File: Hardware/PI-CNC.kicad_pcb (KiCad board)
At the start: 4 copper layers, 65 x 56 mm, 18 parts, among them J3 40HAT, J6 CONN_02X02, J9 CONN_01X02, Q1 DMG2305UX, Q2 DMMT5401, U2 CAT24C32

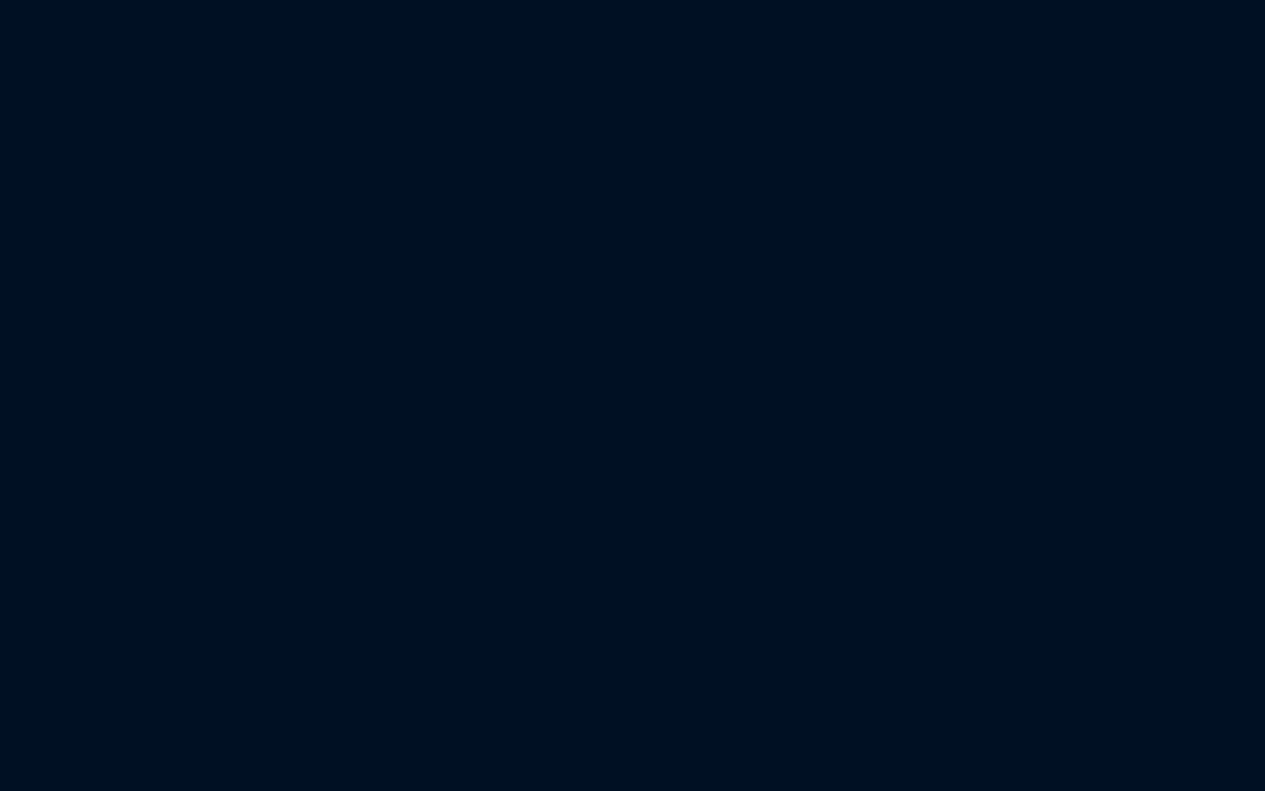
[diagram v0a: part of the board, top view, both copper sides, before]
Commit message: Main Parts on schematic and board.
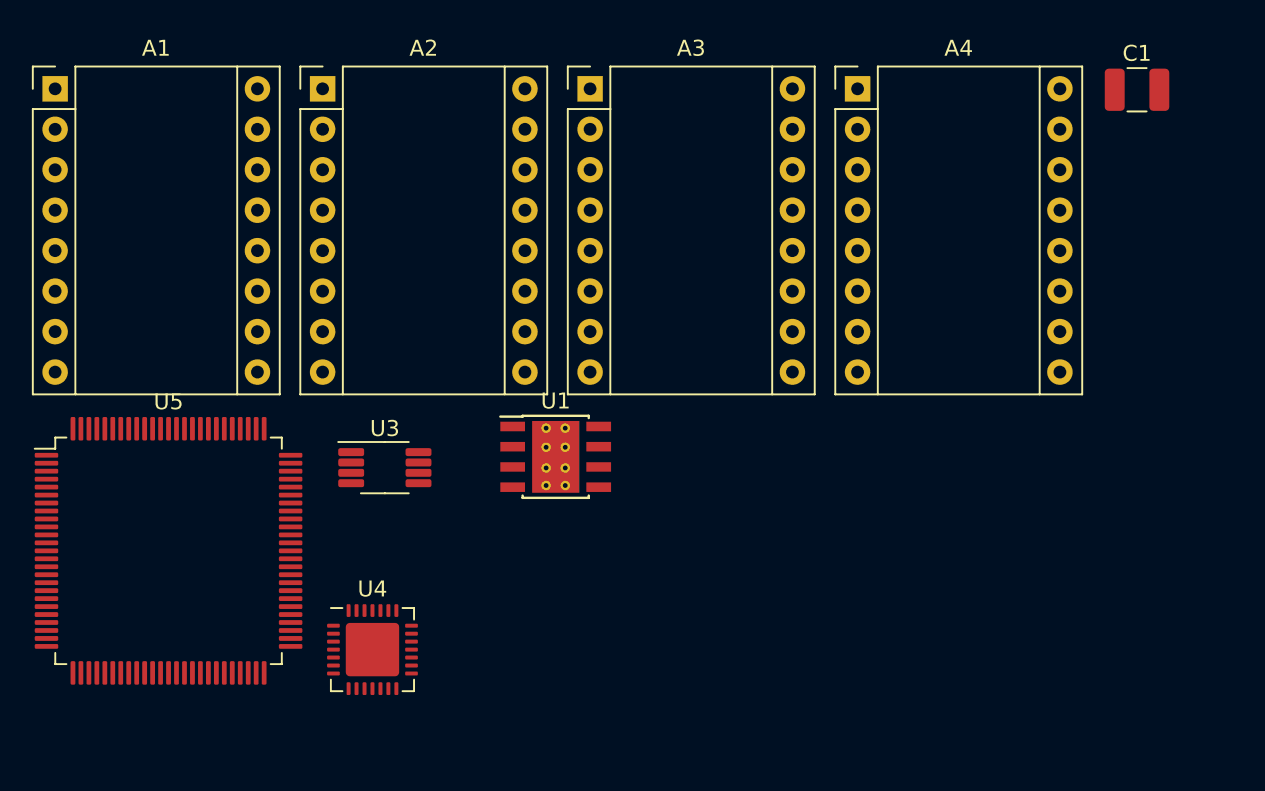
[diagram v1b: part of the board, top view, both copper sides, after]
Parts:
- added A1: Pololu_Breakout_A4988, Module:Pololu_Breakout-16_15.2x20.3mm, F.Cu at (62.6, 18.7)
- added A2: Pololu_Breakout_A4988, Module:Pololu_Breakout-16_15.2x20.3mm, F.Cu at (79.4, 18.7)
- added A3: Pololu_Breakout_A4988, Module:Pololu_Breakout-16_15.2x20.3mm, F.Cu at (96.2, 18.7)
- added A4: Pololu_Breakout_A4988, Module:Pololu_Breakout-16_15.2x20.3mm, F.Cu at (113.0, 18.7)
- added C1: C, Capacitor_SMD:C_1210_3225Metric, F.Cu at (130.5, 18.8)
- added U1: TPS54360DDA, Package_SO:TI_SO-PowerPAD-8_ThermalVias, F.Cu at (94.1, 41.8)
- added U3: DS1339+, Package_SO:MSOP-8_3x3mm_P0.65mm, F.Cu at (83.3, 42.5)
- added U4: CP2102N-A01-GQFN28, Package_DFN_QFN:QFN-28-1EP_5x5mm_P0.5mm_EP3.35x3.35mm, F.Cu at (82.6, 53.9)
- added U5: ATmega2560-16AU, Package_QFP:TQFP-100_14x14mm_P0.5mm, F.Cu at (69.8, 47.7)
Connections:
- J3 pad 10: (no net) -> Console_RX
- J3 pad 11: (no net) -> Net-(J3-Pad11)
- J3 pad 12: (no net) -> LED_white
- J3 pad 13: (no net) -> Net-(J3-Pad13)
- J3 pad 15: (no net) -> Net-(J3-Pad15)
- J3 pad 16: (no net) -> LED_red
- J3 pad 17: (no net) -> Net-(J3-Pad17)
- J3 pad 18: (no net) -> LED_green
- J3 pad 19: (no net) -> Net-(J3-Pad19)
- J3 pad 2: /P5V_HAT -> +5V
- J3 pad 21: (no net) -> Input_SW3
- J3 pad 22: (no net) -> LED_blue
- J3 pad 23: (no net) -> Net-(J3-Pad23)
- J3 pad 24: (no net) -> Net-(J3-Pad24)
- J3 pad 26: (no net) -> Net-(J3-Pad26)
- J3 pad 29: (no net) -> Input_SW2
- J3 pad 3: (no net) -> Net-(J3-Pad3)
- J3 pad 31: (no net) -> UC_Reset
- J3 pad 32: (no net) -> Data_to_UC
- J3 pad 33: (no net) -> Data_from_UC
- J3 pad 35: (no net) -> Net-(J3-Pad35)
- J3 pad 36: (no net) -> Net-(J3-Pad36)
- J3 pad 37: (no net) -> Net-(J3-Pad37)
- J3 pad 38: (no net) -> Net-(J3-Pad38)
- J3 pad 4: /P5V_HAT -> +5V
- J3 pad 40: (no net) -> Net-(J3-Pad40)
- J3 pad 5: (no net) -> Net-(J3-Pad5)
- J3 pad 7: (no net) -> Input_SW1
- J3 pad 8: (no net) -> Console_TX
